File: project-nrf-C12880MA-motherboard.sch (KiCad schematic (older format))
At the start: 34 parts, among them J1 Left, J2 Right, J3 PJ-036AH-SMT-TR, J4 SM04B-SRSS-TB(LF)(SN), J5 SM04B-SRSS-TB(LF)(SN), J6 SM04B-SRSS-TB(LF)(SN), J7 1702473, J8 C12880MA Breakboard v2, U1 ADS1219IPWR, U2 TPS7A0350PDBVR

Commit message: Change ADC to dual OpAmp
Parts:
- removed C1, C5: 0.1uF, Capacitor_SMD:C_0603_1608Metric, symbol Device:C_Small
- removed J8: C12880MA Breakboard v2, 15650122601000, symbol 15650122601000:15650122601000
- removed JP1: SolderJumper_3_Bridged12, Jumper:SolderJumper-3_P1.3mm_Bridged12_RoundedPad1.0x1.5mm, symbol Jumper:SolderJumper_3_Bridged12
- removed U1: ADS1219IPWR, SOP65P640X120-16N, symbol ADS1219IPWR:ADS1219IPWR
- removed U?: LMV792MM, SOP50P490X110-10N, symbol LMV792MM:LMV792MM
- gave numbers to parts that had none: 6
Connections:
- net 5V_FOLLOWER_OUT is gone; now on an unnamed net: R2.1
- net +5V: now also U1.10 (V+), U1.5 (EN), U1.6 (EN)
- net 0.13: now also U1.8 (-), U1.9
- net GND: now also U1.4 (V-)
- net VIDEO: now also U1.3 (+)
- net at R2.2, R3.1, R4.1: now also U1.7 (+)
- net at U1.1: now also U1.2 (-)
- no-connect marks 12 -> 9
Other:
- note removed: "Default I2c address: 0x40"
- note removed: "I2C address: 0x40 || 0x44"
- moved on the sheet: C4, IC1, R2, R3, R4, U1A, U1B, U1C

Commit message: Routing done
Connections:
- net 0.09: now also J6.2; no longer J6.3
- net 0.10: now also J6.3; no longer J6.2
- net 0.13: now also J7.1, R1.2, S1.1, S1.2; no longer U1.8 (-), U1.9
- net 0.31: now also U1.8 (-), U1.9; no longer J7.1, R1.2, S1.1, S1.2
- net CLK: now also IC1.12 (B2Y); no longer IC1.13 (B1Y)
- net START: now also IC1.13 (B1Y); no longer IC1.12 (B2Y)
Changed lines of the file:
@@
 Wire Wire Line
 	7550 1300 7700 1300
+Text Label 2500 2650 2    50   ~ 0
+RX
 Text Label 2500 2550 2    50   ~ 0
-RX
-Text Label 2500 2650 2    50   ~ 0
 TX
 Wire Wire Line
@@
 Wire Wire Line
 	1850 3350 2500 3350
-Text Label 2500 3350 2    50   ~ 0
+Text Label 1500 3050 2    50   ~ 0
 ADC_INPUT
 Wire Wire Line
@@
 	1    0    0    -1
 $EndComp
-Text Label 1500 3050 2    50   ~ 0
+Text Label 2500 3350 2    50   ~ 0
 BUTTON
 Wire Wire Line
@@
 Wire Wire Line
 	9800 4900 9550 4900
+Text Label 9800 5000 2    50   ~ 0
+CLK
+Wire Wire Line
+	9800 5000 9550 5000
 Text Label 9800 4900 2    50   ~ 0
-CLK
-Wire Wire Line
-	9800 5000 9550 5000
-Text Label 9800 5000 2    50   ~ 0
 START
 Text Label 9800 5200 2    50   ~ 0

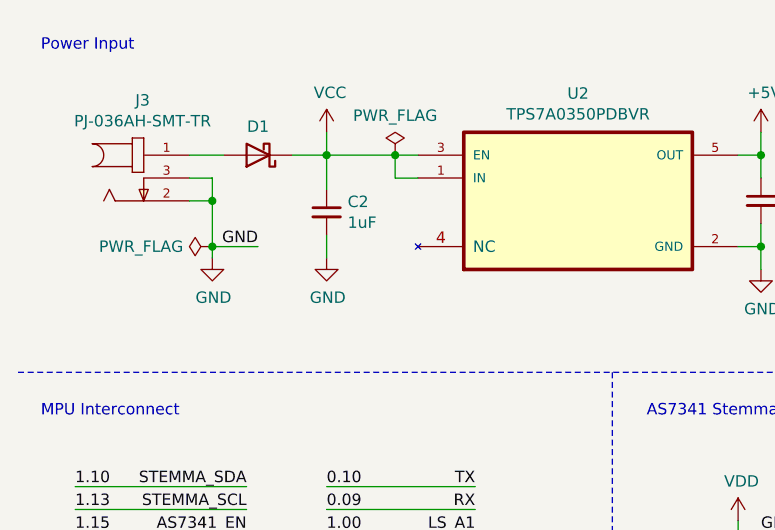
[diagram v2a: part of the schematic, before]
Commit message: Reroute regulator section and fix cap footprint (0603->0805)
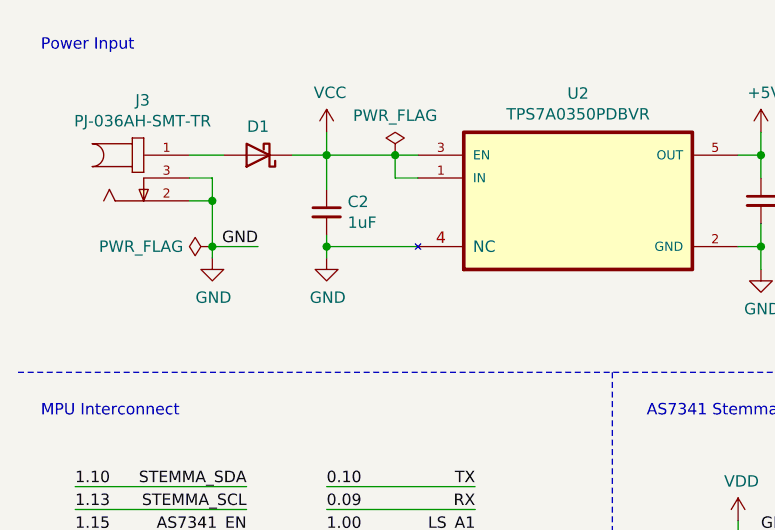
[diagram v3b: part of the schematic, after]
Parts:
- C2, C3: footprint Capacitor_SMD:C_0603_1608Metric -> Capacitor_SMD:C_0805_2012Metric
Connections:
- net GND: now also U2.4 (NC)
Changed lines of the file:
@@
 F 0 "C2" H 1942 1396 50  0000 L CNN
 F 1 "1uF" H 1942 1305 50  0000 L CNN
-F 2 "Capacitor_SMD:C_0603_1608Metric" H 1850 1350 50  0001 C CNN
+F 2 "Capacitor_SMD:C_0805_2012Metric" H 1850 1350 50  0001 C CNN
 F 3 "~" H 1850 1350 50  0001 C CNN
 	1    1850 1350
@@
 F 0 "C3" H 3842 1346 50  0000 L CNN
 F 1 "1uF" H 3842 1255 50  0000 L CNN
-F 2 "Capacitor_SMD:C_0603_1608Metric" H 3750 1300 50  0001 C CNN
+F 2 "Capacitor_SMD:C_0805_2012Metric" H 3750 1300 50  0001 C CNN
 F 3 "~" H 3750 1300 50  0001 C CNN
 	1    3750 1300
@@
 $EndComp
 Wire Wire Line
-	1850 1450 1850 1550
+	1850 1450 1850 1500
 $Comp
 L power:PWR_FLAG #FLG0102
@@
 Wire Wire Line
 	5100 1400 5100 1700
+Wire Wire Line
+	2250 1500 1850 1500
+Connection ~ 1850 1500
+Wire Wire Line
+	1850 1500 1850 1550
 $EndSCHEMATC

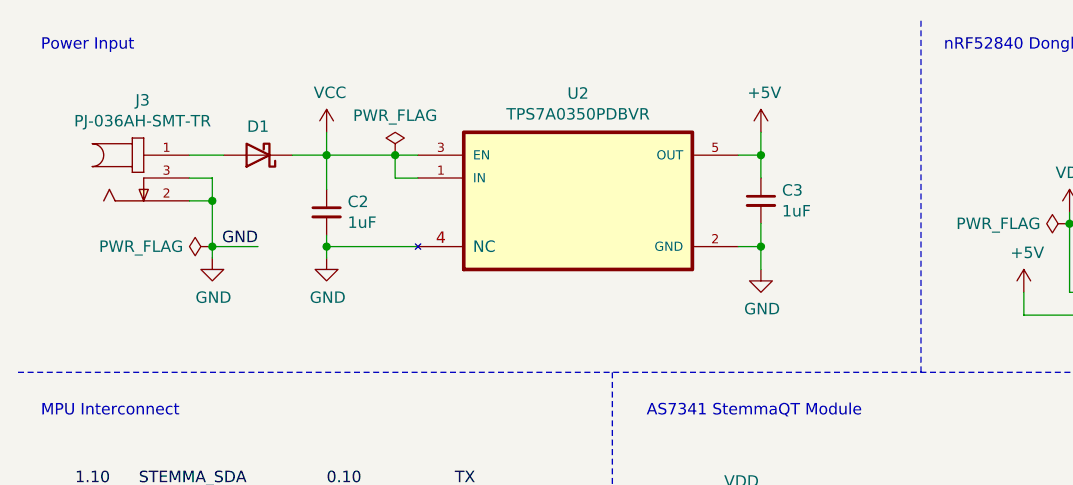
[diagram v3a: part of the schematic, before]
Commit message: Swap the regulator for the LP2985-50
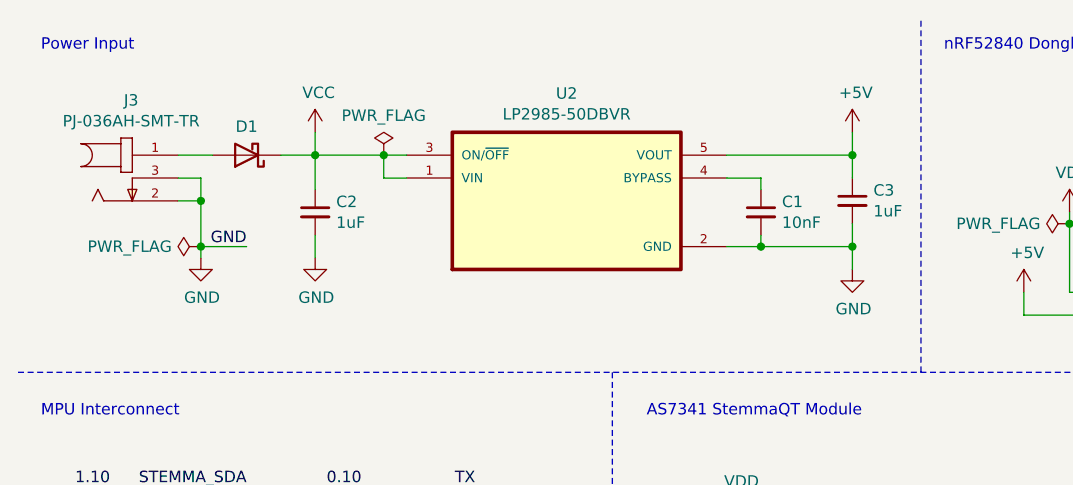
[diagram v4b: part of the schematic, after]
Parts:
- removed U2: TPS7A0350PDBVR, SOT95P280X145-5N, symbol TPS7A0233PDBVR:TPS7A0233PDBVR
- added C1: 10nF, Capacitor_SMD:C_0603_1608Metric, symbol Device:C_Small
- added U2: LP2985-50DBVR, SOT95P280X145-5N, symbol LP2985-50DBVR:LP2985-50DBVR
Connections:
- net +5V: now also U2.5 (VOUT)
- net GND: now also C1.2, U2.2 (GND)
- net VCC: now also U2.1 (VIN), U2.3 (ON/~OFF)
- new net: C1.1, U2.4 (BYPASS)
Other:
- moved on the sheet: C2, C3, D1, J3
